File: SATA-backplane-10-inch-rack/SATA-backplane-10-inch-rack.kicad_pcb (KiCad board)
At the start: 2 copper layers, 210.1 x 69.6 mm, 37 parts, among them J101 Conn_01x06, J201 67800-5001, J202 1735284-2, J301 67800-5001, J302 1735284-2, J401 67800-5001, J402 1735284-2, J501 67800-5001, J502 1735284-2, J601 67800-5001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

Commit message: Place & Route
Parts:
- JP101, JP102: value SolderJumper -> Jumper; footprint Jumper:SolderJumper-2_P1.3mm_Open_RoundedPad1.0x1.5mm -> Connector_PinHeader_2.54mm:PinHeader_1x02_P2.54mm_Horizontal
- moved D104 116.0 mm to (35.2, 114.9)
- moved Q101 116.0 mm to (37.7, 110.2)
- moved R102 116.0 mm to (35.2, 103.6)
- moved Q102 116.0 mm to (38.0, 106.9)
- moved R103 116.0 mm to (39.3, 103.6)
- moved R104 116.0 mm to (37.2, 103.6)
- moved R105 116.0 mm to (37.3, 99.1)
- moved JP101 96.9 mm to (126.7, 116.5), turned to 90 degrees
- moved R101 93.5 mm to (133.0, 117.6), turned to 0 degrees
- moved C104 85.5 mm to (133.6, 115.0), turned to 180 degrees
- moved U1 81.1 mm to (169.6, 114.1), turned to 90 degrees
- moved JP102 80.0 mm to (160.7, 116.4), turned to 90 degrees
- moved C101 70.2 mm to (166.4, 143.2)
- moved D102 70.2 mm to (167.4, 130.7)
- moved C102 70.2 mm to (165.1, 134.0)
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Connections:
- C104 pad 2: Net-(JP101-A) -> Net-(JP101-B)
- J101 pad 1: +3.3V -> GND
- J101 pad 2: GND -> +3.3V
- J101 pad 3: +5V -> GND
- J101 pad 4: GND -> +5V
- J101 pad 5: +12V -> GND
- J101 pad 6: GND -> +12V
- JP101 pad 1: Net-(JP101-A) -> STA_N
- JP101 pad 2: STA_N -> Net-(JP101-B)
- JP102 pad 1: Net-(JP102-A) -> +3.3V
- JP102 pad 2: +3.3V -> Net-(JP102-B)
- R101 pad 1: Net-(JP101-A) -> Net-(JP101-B)
- U1 pad 2: Net-(JP102-A) -> Net-(JP102-B)
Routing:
- net ACT: track 0.00 -> 280.2 mm
- net STA_N: track 0.00 -> 207.6 mm
- net +5V: track 0.00 -> 54.3 mm, vias 4 -> 10
- net +3.3V: track 0.00 -> 52.7 mm, vias 4 -> 5
- net /Port_6/STA/ACT: track 29.9 -> 4.66 mm, vias 4 -> 1
- net Net-(JP102-B): track 0.00 -> 13.6 mm
- net Net-(JP101-A): track 8.01 -> 0.00 mm
- net Net-(JP101-B): track 0.00 -> 6.01 mm
- net GND: track 120.9 -> 122.0 mm, vias 155 -> 150
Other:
- board text added: "1"
- board text added: "2"
- board text added: "3"
- board text added: "4"
- board text added: "5"
- board text added: "6"

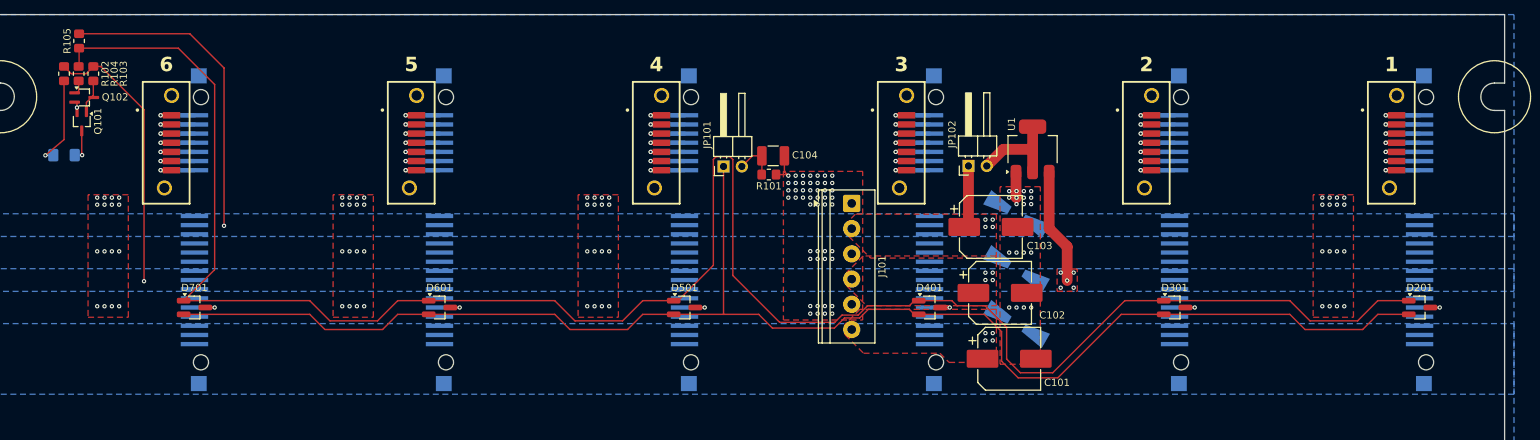
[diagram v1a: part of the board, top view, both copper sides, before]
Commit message: Finish layout
Plus backport 3D into KiCAD
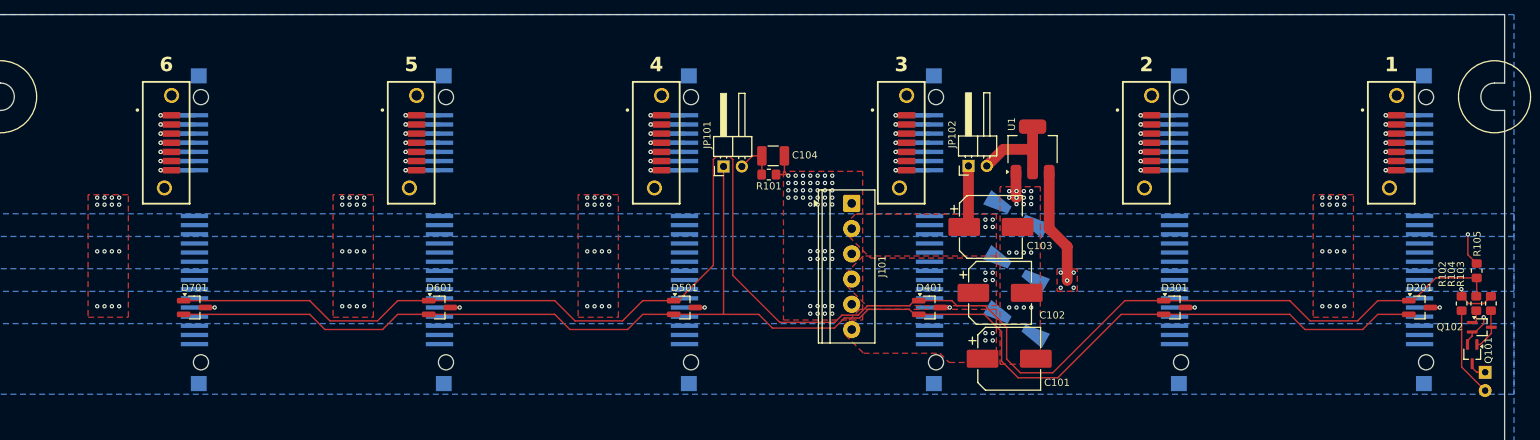
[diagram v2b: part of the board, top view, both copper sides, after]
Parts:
- added Ref**: BOM_additional_purcase_order, Kharars-KiCAD-lib:BOM_additional_purcase_order, F.Cu at (25.0, 165.0)
- D104: footprint LED_SMD:LED_1206_3216Metric_Pad1.42x1.75mm_HandSolder -> LED_THT:LED_D3.0mm_Clear
- moved D104 199.5 mm to (232.4, 145.0), turned to -90 degrees
- moved Q102 196.5 mm to (231.9, 138.8)
- moved R104 196.5 mm to (231.2, 135.5)
- moved R102 196.5 mm to (229.1, 135.5)
- moved R103 196.5 mm to (233.2, 135.5)
- moved R105 196.5 mm to (231.2, 130.9)
- moved Q101 195.6 mm to (230.6, 142.5)
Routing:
- net ACT: track 280.2 -> 238.2 mm
- net +3.3V: track 52.7 -> 13.3 mm
- net +5V: track 54.3 -> 22.0 mm
- net GND: track 122.0 -> 125.3 mm
- net Net-(D104-K): track 5.19 -> 2.63 mm, vias 1 -> 0
- net Net-(Q101-G): track 5.00 -> 5.82 mm
- net Net-(D104-A): track 13.1 -> 12.4 mm, vias 1 -> 0
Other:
- board text added: "ACT"
- board text removed: "ACTIVITY"
